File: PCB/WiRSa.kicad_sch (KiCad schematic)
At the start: 3 parts

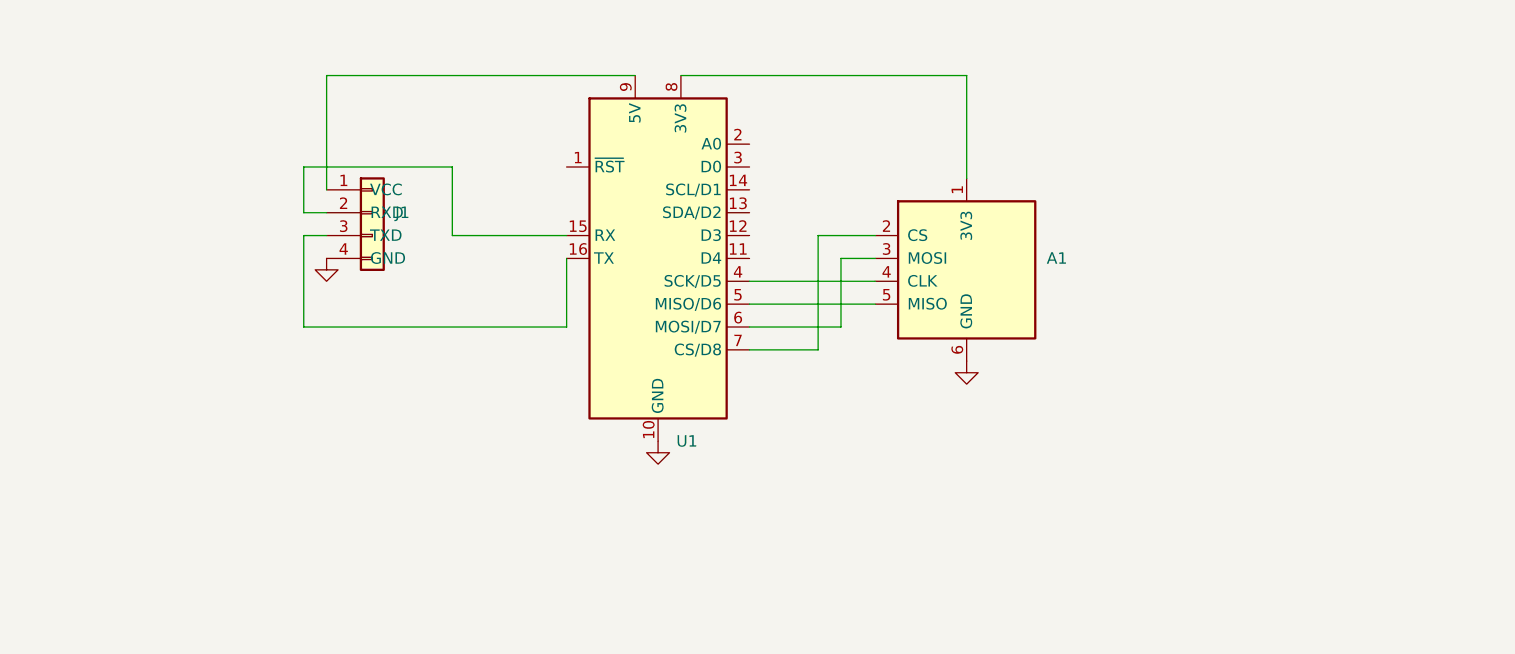
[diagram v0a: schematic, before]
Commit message: v2 PCB update
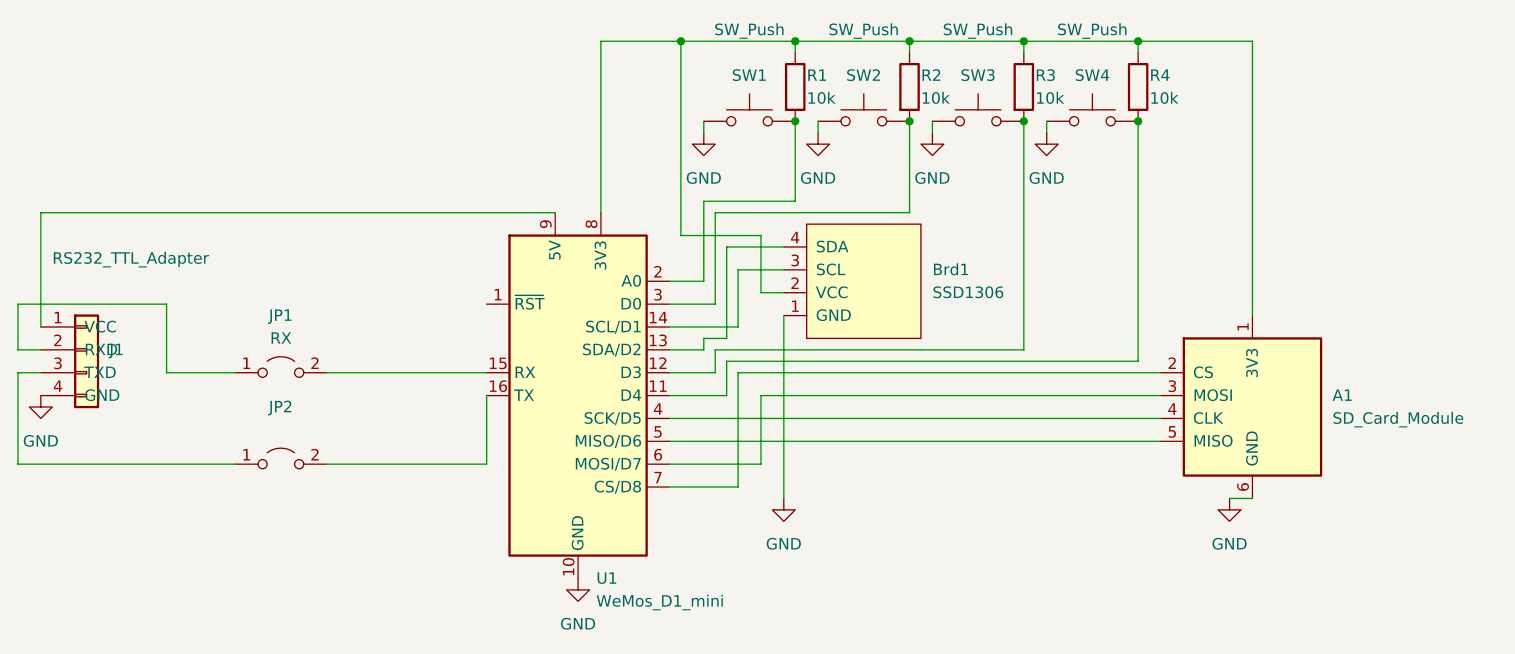
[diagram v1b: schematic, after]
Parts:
- added Brd1: SSD1306, SSD1306:128x64OLED, symbol SSD1306:SSD1306
- added JP1: RX, TestPoint:TestPoint_2Pads_Pitch2.54mm_Drill0.8mm, symbol Jumper:Jumper_2_Open
- added JP2: (no value), symbol Jumper:Jumper_2_Open
- added R1, R2, R3, R4: 10k, Resistor_THT:R_Axial_DIN0207_L6.3mm_D2.5mm_P7.62mm_Horizontal, symbol Device:R
- added SW1, SW2, SW3, SW4: SW_Push, Button_Switch_THT:SW_Tactile_SPST_Angled_PTS645Vx58-2LFS, symbol Switch:SW_Push
- A1: value (none) -> SD_Card_Module; footprint (none) -> Charleslabs_Parts:SD_Card_Module
- J1: value (none) -> RS232_TTL_Adapter; footprint (none) -> Connector_PinHeader_2.54mm:PinHeader_1x04_P2.54mm_Vertical
- U1: value (none) -> WeMos_D1_mini; footprint (none) -> Module:WEMOS_D1_mini_light
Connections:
- net GND: now also Brd1.1 (GND), SW1.1, SW2.1, SW3.1, SW4.1
- net at U1.11 (D4): now also R4.2, SW4.2
- net at U1.12 (D3): now also R3.2, SW3.2
- net at U1.13 (SDA/D2): now also Brd1.4 (SDA)
- net at U1.14 (SCL/D1): now also Brd1.3 (SCL)
- net at U1.15 (RX): now also JP1.2 (B); no longer J1.2 (RXD)
- net at U1.16 (TX): now also JP2.2 (B); no longer J1.3 (TXD)
- net at U1.2 (A0): now also R1.2, SW1.2
- net at U1.3 (D0): now also R2.2, SW2.2
- net at A1.1 (3V3), U1.8 (3V3): now also Brd1.2 (VCC), R1.1, R2.1, R3.1, R4.1
- new net: J1.3 (TXD), JP2.1 (A)
- new net: J1.2 (RXD), JP1.1 (A)
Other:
- moved on the sheet: A1, J1, U1

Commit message: WiRSa v3.01
Initial push for the version 3 design
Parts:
- removed A1: SD_Card_Module, Charleslabs_Parts:SD_Card_Module, symbol Charles:SD_Card_Module
- removed Brd1: SSD1306, SSD1306:128x64OLED, symbol SSD1306:SSD1306
- removed J1: RS232_TTL_Adapter, Connector_PinHeader_2.54mm:PinHeader_1x04_P2.54mm_Vertical, symbol Connector_Generic:Conn_01x04
- removed JP1: RX, TestPoint:TestPoint_2Pads_Pitch2.54mm_Drill0.8mm, symbol Jumper:Jumper_2_Open
- removed JP2: (no value), symbol Jumper:Jumper_2_Open
- removed U1: WeMos_D1_mini, Module:WEMOS_D1_mini_light, symbol MCU_Module:WeMos_D1_mini
- added C1, C2, C3, C4, C5: 0.1uF, Capacitor_SMD:C_0603_1608Metric, symbol Device:C_Small
- added IC1: MAX3243CDBR, easyeda2kicad:SSOP-28_L10.2-W5.3-P0.65-LS7.8-BL, symbol SamacSys:MAX3243CUI+
- added J1: DE9 Female, Connector_Dsub:DSUB-9_Female_Horizontal_P2.77x2.84mm_EdgePinOffset4.94mm_Housed_MountingHolesOffset7.48mm, symbol Connector:DE9_Receptacle_MountingHoles
- added J2: spare IO, Connector_PinHeader_2.54mm:PinHeader_1x02_P2.54mm_Vertical, symbol Connector:Conn_01x02_Pin
- added J3: Conn_01x02_Socket, Connector_PinHeader_2.54mm:PinHeader_1x02_P2.54mm_Vertical, symbol Connector:Conn_01x02_Socket
- added J4: 2016WVS-02P, easyeda2kicad:CONN-SMD_P2.00_X2016WVS-02-9TSW, symbol easyeda2kicad:2016WVS-02P
- added R5, R6, R7, R8, R9: 10k, Resistor_SMD:R_0603_1608Metric, symbol Device:R
- added SW5: SK-3245S-L3-B, easyeda2kicad:SW-SMD_SK-3245S-L3-B, symbol easyeda2kicad:SK-3245S-L3-B
- added U1: TF-123-ARP9H17, easyeda2kicad:TF-SMD_TF-123-ARP9H15, symbol easyeda2kicad:TF-123-ARP9H17
- added U2: ESP32-WROOM-32D DEV BOARD, esp32:ESP32-C3-DevKitC-02, symbol RF_Module:ESP32-WROOM-32D
- R1, R2, R3, R4: footprint Resistor_THT:R_Axial_DIN0207_L6.3mm_D2.5mm_P7.62mm_Horizontal -> Resistor_SMD:R_0603_1608Metric; LCSC (none) -> C25804
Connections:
- net GND: now also C3.2, C4.2, C5.2, IC1.25 (GND), J1.5, J4.3, J4.4, U1.10, U1.11, U1.12, U1.13, U1.6 (VSS), U2.2 (GND), U2.29 (GND)
- net at R4.2, SW4.2: now also U2.20 (D35)
- net at R3.2, SW3.2: now also U2.19 (D34)
- net at R1.2, SW1.2: now also U2.17 (D36/SENS_VP)
- net at R2.2, SW2.2: now also U2.18 (D39/SENS_VN)
- net at R1.1, R2.1, R3.1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: now also C4.1, IC1.22 (~{FORCEOFF}), IC1.23 (FORCEON), IC1.26 (VCC), R5.1, R6.1, R7.1, R8.1, R9.1, U1.4 (VDD), U2.1 (3.3V)
- new net: R7.2, U1.3 (CMD), U2.15 (D23/VMOSI)
- new net: J4.1, SW5.2
- new net: J4.2, SW5.5
- new net: R6.2, U1.7 (DAT0), U2.10 (D19/VMISO)
- new net: C2.1, IC1.1 (C2+)
- new net: C2.2, IC1.2 (C2-)
- new net: C1.2, IC1.24 (C1-)
- new net: C3.1, IC1.27 (V+)
- new net: C1.1, IC1.28 (C1+)
- new net: C5.1, IC1.3 (V-)
- new net: J3.1 (Pin_1), SW5.1
- new net: J3.2 (Pin_2), SW5.4
- new net: R5.2, U1.8 (DAT1)
- new net: U1.9 (SWITCH), U2.26 (D14/HCLK)
- new net: J2.1 (Pin_1), U2.27 (D12/HMISO)
- new net: J2.2 (Pin_2), U2.28 (D13/HMOSI)
- new net: R8.2, U1.2 (CD/DAT3), U2.8 (D5/VCS)
- new net: U1.5 (CLK), U2.9 (D18/VCLK)
- new net: R9.2, U1.1 (DAT2)
- new net CTS-RI: IC1.7 (R4IN), J1.8
- new net CTS-TO: IC1.16 (R4OUT), U2.25 (D27)
- new net DCD-RI: IC1.4 (R1IN), J1.1
- new net DCD-TO: IC1.19 (R1OUT), U2.22 (D33)
- new net DSR-RI: IC1.6 (R3IN), J1.6
- new net DSR-TO: IC1.17 (R3OUT), U2.24 (D26)
- new net DTR-RO: IC1.10 (T2OUT), J1.4
- new net DTR-TI: IC1.13 (T2IN), U2.5 (D4)
- new net RI in standby mode??: IC1.20 (R2OUTB)
- new net RI-RI: IC1.5 (R2IN), J1.9
- new net RI-TO: IC1.18 (R2OUT), U2.23 (D25)
- new net RTS-RO: IC1.11 (T3OUT), J1.7
- new net RTS-TI: IC1.12 (T3IN), U2.3 (D15/HCS)
- new net RX-RI: IC1.8 (R5IN), J1.3
- new net RX-TO: IC1.15 (R5OUT), U2.6 (D16/RX2)
- new net TX-RO: IC1.9 (T1OUT), J1.2
- new net TX-TI: IC1.14 (T1IN), U2.7 (D17/TX2)
- new net /INVALID: IC1.21 (~{INVALID}), U2.21 (D32)
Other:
- note added: "0"
- note added: "WiRSa V3"
